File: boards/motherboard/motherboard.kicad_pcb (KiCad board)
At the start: 2 copper layers, 214.4 x 66 mm, 50 parts, among them J1 RJ45, J2 RJ45, J3 RJ45, J4 RJ45, J5 RJ45, U1 EBAYPCA9685

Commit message: another revision
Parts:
- added REF11: MountingHole_2-5mm, Mounting_Holes:MountingHole_2-5mm, F.Cu at (66.3, 49.5)
- 350ma1, 350ma10, 350ma11, 350ma12, 350ma13, 350ma14, 350ma15, 350ma2, 350ma3, 350ma4, 350ma5, 350ma6, 350ma7, 350ma8, 350ma9: footprint lighting:350ma constant current xl4001 -> lighting:350ma_constant_current_xl4001
- BLK1, BLK2: footprint lighting:TerminalBlock -> Connect:bornier2
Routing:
- net GNDPWR: track 100.2 -> 93.4 mm
- net +24V: track 98.8 -> 97.6 mm
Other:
- board text added: "0"
- board text added: "1"
- board text added: "2"
- board text added: "3"
- board text added: "4"

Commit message: minor fix
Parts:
- moved REF3 3.05 mm to (232.7, 49.5)
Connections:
- R12 pad 1: Net-(R12-Pad1) -> VCC
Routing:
- net /led0: track 77.0 -> 79.5 mm
- net VCC: track 273.6 -> 275.4 mm
- net /scl: track 73.0 -> 73.9 mm

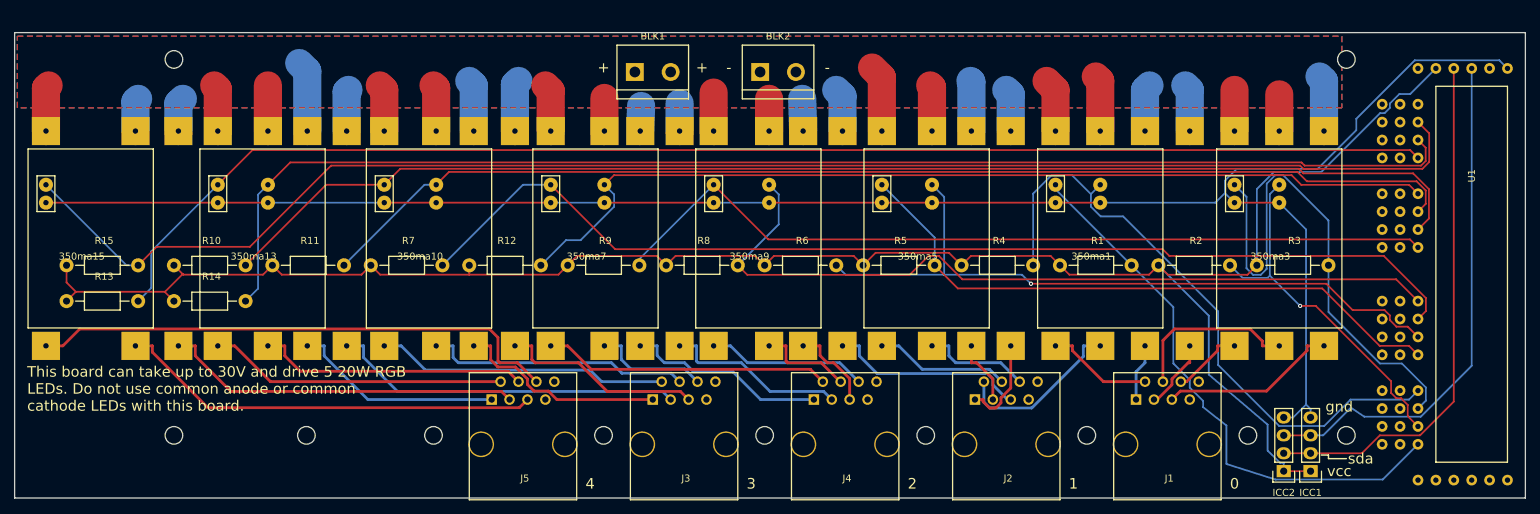
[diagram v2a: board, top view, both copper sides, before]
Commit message: added breakout for ethernet
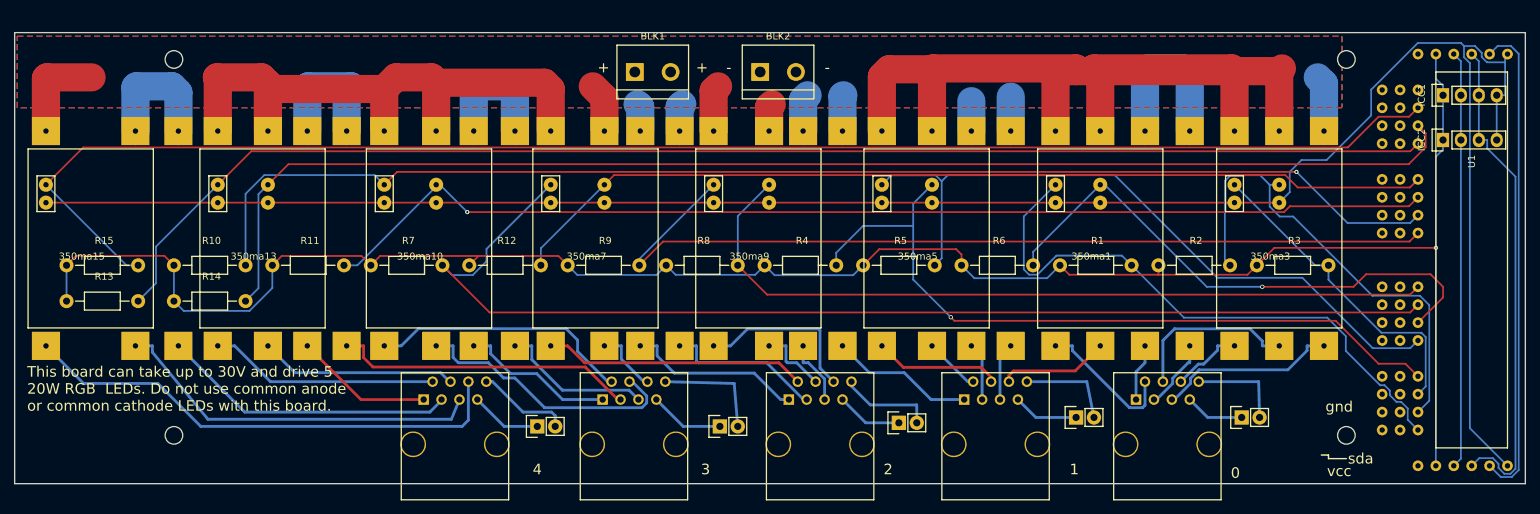
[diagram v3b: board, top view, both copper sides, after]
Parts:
- removed REF1, REF4, REF5, REF6, REF7, REF8, REF9: MountingHole_2-5mm, Mounting_Holes:MountingHole_2-5mm
- added CN1: CONN_01X02, Pin_Headers:Pin_Header_Straight_1x02, F.Cu at (217.8, 100.3)
- added CN2: CONN_01X02, Pin_Headers:Pin_Header_Straight_1x02, F.Cu at (194.3, 100.3)
- added CN3: CONN_01X02, Pin_Headers:Pin_Header_Straight_1x02, F.Cu at (143.8, 101.6)
- added CN4: CONN_01X02, Pin_Headers:Pin_Header_Straight_1x02, F.Cu at (169.2, 101.1)
- added CN5: CONN_01X02, Pin_Headers:Pin_Header_Straight_1x02, F.Cu at (117.9, 101.6)
- moved ICC1 56.6 mm to (246.4, 54.6), turned to 90 degrees
- moved ICC2 52.1 mm to (246.4, 61.0), turned to 90 degrees
- moved R4 27.9 mm to (150.1, 78.7)
- moved R6 27.9 mm to (178.1, 78.7)
- moved 350ma4 23.9 mm to (173.9, 90.2)
- moved 350ma6 23.9 mm to (197.7, 90.2)
- moved J5 9.65 mm to (106.2, 104.1)
- moved J3 7.11 mm to (131.6, 104.1)
- moved J4 3.56 mm to (158.0, 104.1)
- moved U1 2.03 mm to (237.7, 53.8)
- moved J2 1.52 mm to (182.9, 104.1)
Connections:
- U1 pad 17: Net-(U1-Pad17) -> V+
- U1 pad 23: (no net) -> V+
- U1 pad 24: (no net) -> VCC
- U1 pad 25: (no net) -> /sda
- U1 pad 26: (no net) -> /scl
- U1 pad 27: (no net) -> Net-(U1-Pad21)
- U1 pad 28: (no net) -> GND
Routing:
- net +24V: track 97.6 -> 246.6 mm
- net Net-(U1-Pad21): track 0.00 -> 69.3 mm
- net GND: track 262.7 -> 297.4 mm
- net /led2: track 74.8 -> 45.8 mm
- net /led5: track 100.6 -> 78.0 mm
- net GNDPWR: track 93.4 -> 114.3 mm
- net Net-(350ma6-Pad4): track 28.4 -> 8.25 mm
- net /led1: track 51.8 -> 68.3 mm, vias 1 -> 0
- net Net-(350ma4-Pad3): track 24.3 -> 7.95 mm
- net /led3: track 90.1 -> 106.2 mm, vias 0 -> 1
- net Net-(CN3-Pad2): track 0.00 -> 15.9 mm
- net /sda: track 74.4 -> 59.3 mm
- net Net-(CN2-Pad2): track 0.00 -> 13.7 mm
- net Net-(CN1-Pad2): track 0.00 -> 13.6 mm
- net Net-(CN4-Pad2): track 0.00 -> 13.6 mm
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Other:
- board size 214.4 x 66 mm -> 214.4 x 64 mm

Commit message: made a hole for capacitor
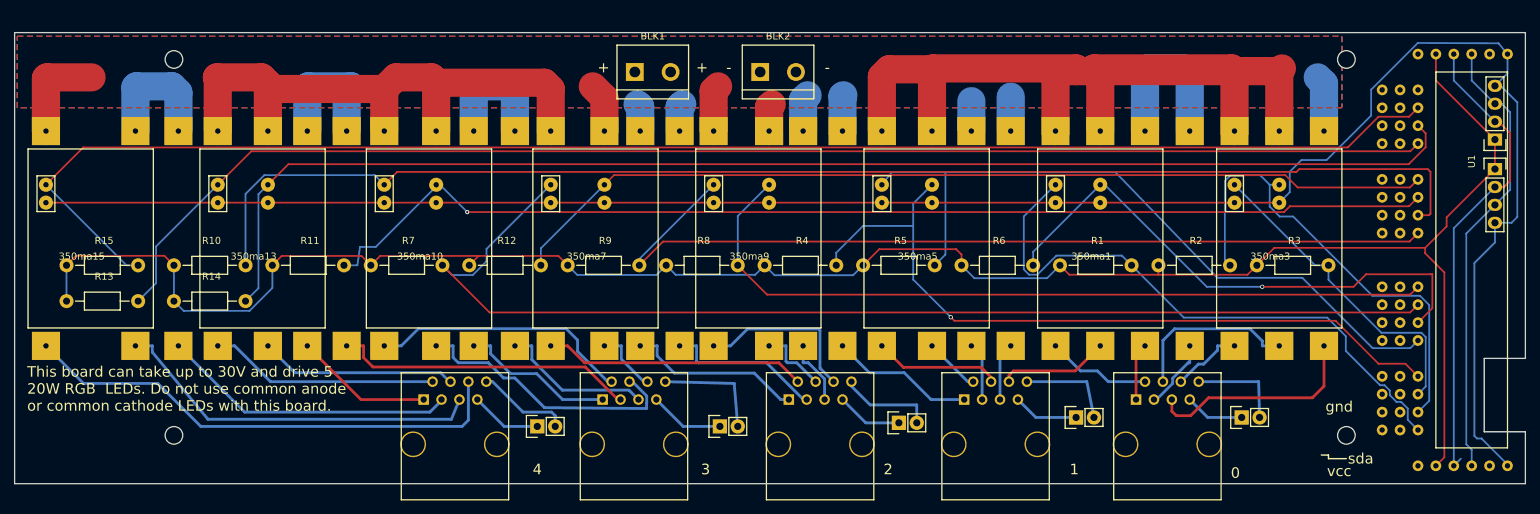
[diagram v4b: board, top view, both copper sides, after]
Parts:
- moved ICC1 9.68 mm to (253.7, 60.9), turned to 180 degrees
- moved ICC2 8.44 mm to (253.7, 65.1), turned to 0 degrees
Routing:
- net Net-(U1-Pad21): track 69.3 -> 0.00 mm
- net GND: track 297.4 -> 289.0 mm
- net /sda: track 59.3 -> 67.5 mm
- net VCC: track 285.2 -> 292.1 mm, vias 1 -> 0
- net /led9: track 182.4 -> 189.1 mm, vias 1 -> 0
- net /scl: track 70.3 -> 64.1 mm
- net Net-(350ma3-Pad4): track 25.6 -> 31.3 mm
- net Net-(350ma1-Pad3): track 20.2 -> 14.8 mm
- net /led4: track 100.3 -> 101.7 mm
- net /led10: track 159.7 -> 160.8 mm
- net /led5: track 78.0 -> 76.9 mm
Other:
- outline, holes or cut-outs redrawn

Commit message: sink
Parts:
- added BLK3: CONN_01X02, Connect:bornier2, F.Cu at (52.1, 105.9)
- REF10, REF11, REF2, REF3: value MountingHole_2-5mm -> MountingHole; footprint Mounting_Holes:MountingHole_2-5mm -> Mounting_Holes:MountingHole_3mm
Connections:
- CN1 pad 1: Net-(CN1-Pad1) -> /gnd2
- CN1 pad 2: Net-(CN1-Pad2) -> /vpwr2
- CN2 pad 1: Net-(CN2-Pad1) -> /gnd2
- CN2 pad 2: Net-(CN2-Pad2) -> /vpwr2
- CN3 pad 1: Net-(CN3-Pad1) -> /gnd2
- CN3 pad 2: Net-(CN3-Pad2) -> /vpwr2
- CN4 pad 1: Net-(CN4-Pad1) -> /gnd2
- CN4 pad 2: Net-(CN4-Pad2) -> /vpwr2
- CN5 pad 1: Net-(CN5-Pad1) -> /gnd2
- CN5 pad 2: Net-(CN5-Pad2) -> /vpwr2
- J1 pad 7: Net-(CN1-Pad1) -> /gnd2
- J1 pad 8: Net-(CN1-Pad2) -> /vpwr2
- J2 pad 7: Net-(CN2-Pad1) -> /gnd2
- J2 pad 8: Net-(CN2-Pad2) -> /vpwr2
- J3 pad 7: Net-(CN3-Pad1) -> /gnd2
- J3 pad 8: Net-(CN3-Pad2) -> /vpwr2
- J4 pad 7: Net-(CN4-Pad1) -> /gnd2
- J4 pad 8: Net-(CN4-Pad2) -> /vpwr2
- J5 pad 7: Net-(CN5-Pad1) -> /gnd2
- J5 pad 8: Net-(CN5-Pad2) -> /vpwr2
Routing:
- net /vpwr2: track 0.00 -> 123.1 mm
- net /gnd2: track 0.00 -> 80.7 mm
- net Net-(CN3-Pad2): track 15.9 -> 0.00 mm
- net Net-(CN2-Pad2): track 13.7 -> 0.00 mm
- net Net-(CN1-Pad2): track 13.6 -> 0.00 mm
- net Net-(CN4-Pad2): track 13.6 -> 0.00 mm
- net Net-(CN5-Pad2): track 13.3 -> 0.00 mm
- net /led0: track 84.0 -> 96.9 mm
- net Net-(CN3-Pad1): track 10.6 -> 0.00 mm
- net Net-(CN5-Pad1): track 10.1 -> 0.00 mm
- net Net-(CN4-Pad1): track 9.37 -> 0.00 mm
- net Net-(CN2-Pad1): track 9.31 -> 0.00 mm
- net Net-(CN1-Pad1): track 8.42 -> 0.00 mm
- net /led2: track 45.8 -> 53.5 mm
- net Net-(350ma9-Pad3): track 24.2 -> 19.2 mm
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- added copper zone on F.Cu, net /gnd2
- added copper zone on B.Cu, net /vpwr2
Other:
- board text added: "scl"
- board text added: "v2+"
- board text added: "v2-"

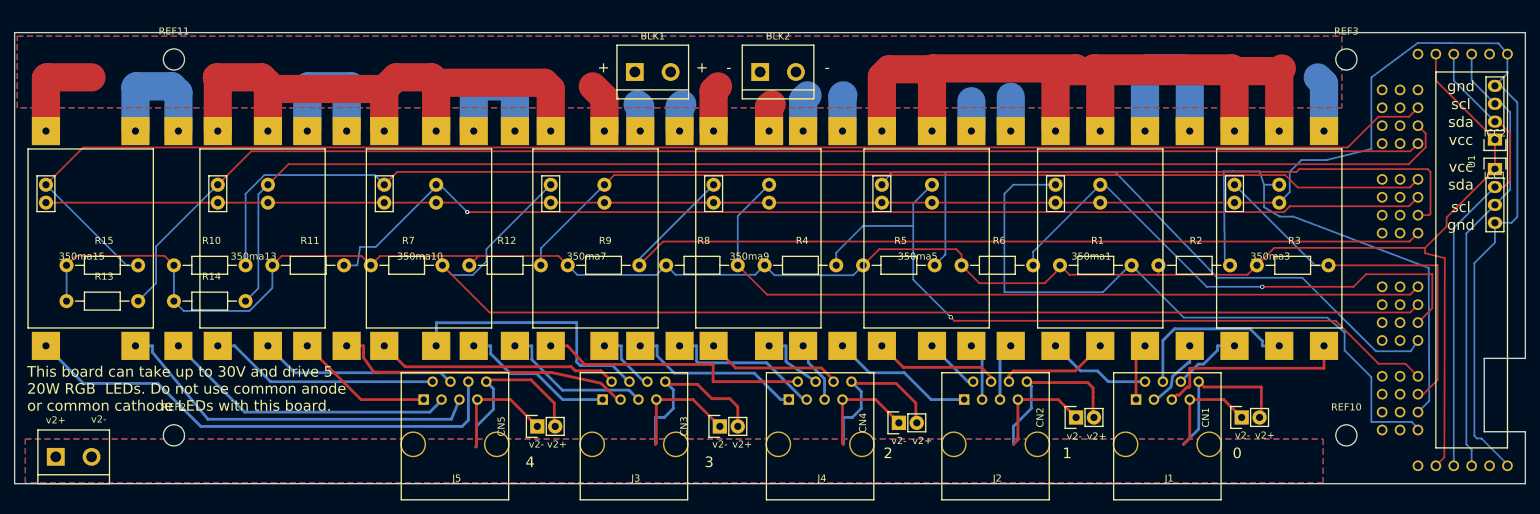
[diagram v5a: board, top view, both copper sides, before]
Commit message: no vias
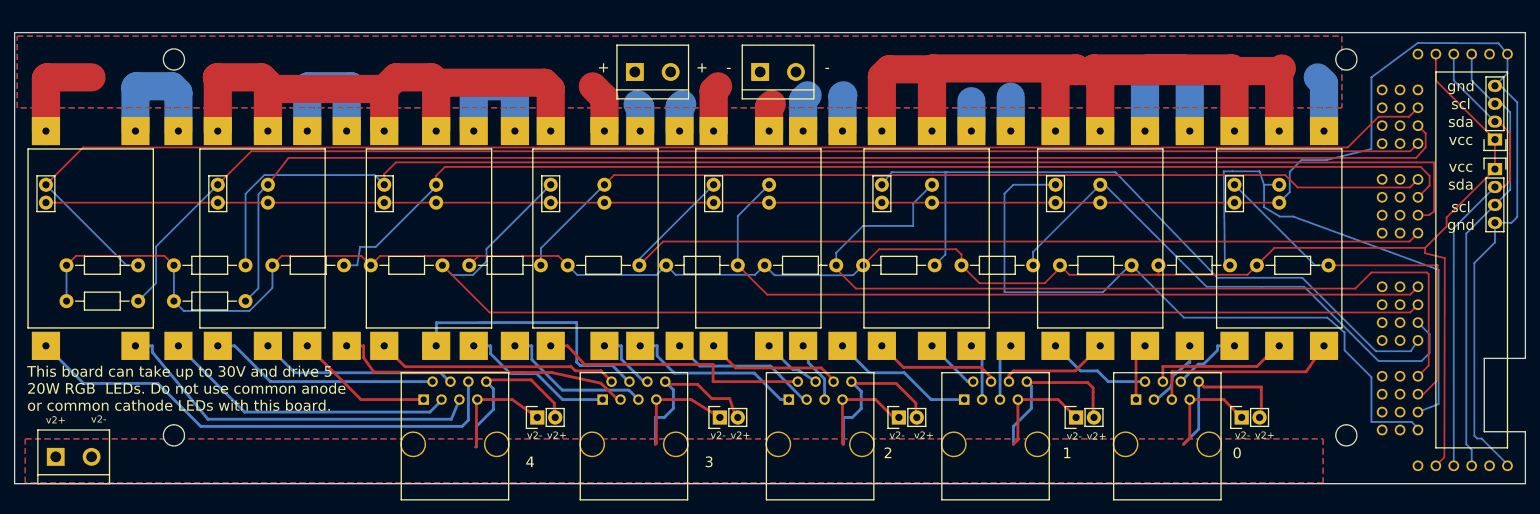
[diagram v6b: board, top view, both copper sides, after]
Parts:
- moved CN3 1.27 mm to (143.8, 100.3)
- moved CN5 1.27 mm to (117.9, 100.3)
- moved CN4 0.76 mm to (169.2, 100.3)
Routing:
- net /led3: track 106.2 -> 123.1 mm, vias 1 -> 0
- net /led10: track 160.8 -> 166.9 mm, vias 1 -> 0
- net Net-(350ma2-Pad3): track 24.4 -> 19.9 mm
- net /led9: track 189.1 -> 192.1 mm
- net /vpwr2: track 123.1 -> 120.2 mm
- net /led1: track 72.2 -> 74.7 mm
- net /gnd2: track 80.7 -> 79.1 mm
- net Net-(350ma8-Pad4): track 22.5 -> 21.2 mm
- net Net-(350ma8-Pad3): track 9.71 -> 8.59 mm
- net /led5: track 76.9 -> 77.9 mm, vias 1 -> 0
- net Net-(350ma3-Pad4): track 28.5 -> 27.8 mm

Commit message: minor changes
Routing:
- net /led13: track 188.2 -> 189.8 mm
- net /led9: track 192.1 -> 193.7 mm
- net VCC: track 293.9 -> 295.5 mm
- net /led1: track 74.7 -> 76.2 mm
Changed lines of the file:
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@@
   (segment (start 220.345 65.405) (end 220.98 67.31) (width 0.25) (layer B.Cu) (net 9))
   (segment (start 216.535 65.405) (end 220.345 65.405) (width 0.25) (layer B.Cu) (net 9))
-  (segment (start 215.265 65.405) (end 216.535 65.405) (width 0.25) (layer B.Cu) (net 9))
-  (segment (start 215.4196 78.0056) (end 215.265 65.405) (width 0.25) (layer B.Cu) (net 9))
-  (segment (start 216.154 78.74) (end 215.4196 78.0056) (width 0.25) (layer B.Cu) (net 9))
+  (segment (start 214.503 65.405) (end 216.535 65.405) (width 0.25) (layer B.Cu) (net 9))
+  (segment (start 214.503 77.978) (end 214.503 65.405) (width 0.25) (layer B.Cu) (net 9))
+  (segment (start 216.154 78.74) (end 214.503 77.978) (width 0.25) (layer B.Cu) (net 9))
   (segment (start 245.745 98.425) (end 242.824 99.568) (width 0.25) (layer B.Cu) (net 9))
   (segment (start 245.745 79.375) (end 245.745 98.425) (width 0.25) (layer B.Cu) (net 9))
@@
   (segment (start 97.79 64.135) (end 96.139 65.786) (width 0.25) (layer F.Cu) (net 31))
   (segment (start 76.454 68.608) (end 76.454 78.74) (width 0.25) (layer B.Cu) (net 31))
-  (segment (start 79.1224 65.9396) (end 76.454 68.608) (width 0.25) (layer B.Cu) (net 31))
-  (segment (start 94.7686 65.9396) (end 79.1224 65.9396) (width 0.25) (layer B.Cu) (net 31))
+  (segment (start 76.454 65.913) (end 76.454 68.608) (width 0.25) (layer B.Cu) (net 31))
+  (segment (start 94.7686 65.9396) (end 76.454 65.913) (width 0.25) (layer B.Cu) (net 31))
   (segment (start 96.139 67.31) (end 94.7686 65.9396) (width 0.25) (layer B.Cu) (net 31))
   (segment (start 103.549537 90.125463) (end 103.549537 86.884895) (width 0.4) (layer B.Cu) (net 32))
@@
   (segment (start 63.7541 76.0729) (end 63.7541 81.2799) (width 0.25) (layer B.Cu) (net 40))
   (segment (start 72.517 67.31) (end 63.7541 76.0729) (width 0.25) (layer B.Cu) (net 40))
-  (segment (start 241.7366 62.5554) (end 242.824 61.468) (width 0.25) (layer F.Cu) (net 40))
-  (segment (start 77.2716 62.5554) (end 241.7366 62.5554) (width 0.25) (layer F.Cu) (net 40))
-  (segment (start 72.517 67.31) (end 77.2716 62.5554) (width 0.25) (layer F.Cu) (net 40))
+  (segment (start 241.808 62.992) (end 242.824 61.468) (width 0.25) (layer F.Cu) (net 40))
+  (segment (start 77.216 62.992) (end 241.808 62.992) (width 0.25) (layer F.Cu) (net 40))
+  (segment (start 72.517 67.31) (end 77.216 62.992) (width 0.25) (layer F.Cu) (net 40))
   (segment (start 105.537 95.25) (end 105.41 95.25) (width 0.4) (layer B.Cu) (net 41))
   (segment (start 105.41 95.25) (end 104.14 93.98) (width 0.4) (layer B.Cu) (net 41))
@@
   (segment (start 79.629 67.31) (end 78.2866 68.6524) (width 0.25) (layer B.Cu) (net 43))
   (segment (start 79.629 67.31) (end 82.55 63.5) (width 0.25) (layer F.Cu) (net 43))
-  (segment (start 243.9134 60.0174) (end 242.824 58.928) (width 0.25) (layer F.Cu) (net 43))
-  (segment (start 243.9134 61.9891) (end 243.9134 60.0174) (width 0.25) (layer F.Cu) (net 43))
-  (segment (start 242.57 63.5) (end 243.9134 61.9891) (width 0.25) (layer F.Cu) (net 43))
+  (segment (start 244.348 59.944) (end 242.824 58.928) (width 0.25) (layer F.Cu) (net 43))
+  (segment (start 244.348 63.5) (end 244.348 59.944) (width 0.25) (layer F.Cu) (net 43))
+  (segment (start 242.57 63.5) (end 244.348 63.5) (width 0.25) (layer F.Cu) (net 43))
   (segment (start 82.55 63.5) (end 242.57 63.5) (width 0.25) (layer F.Cu) (net 43))
   (segment (start 108.077 95.25) (end 108.077 100.711) (width 0.4) (layer B.Cu) (net 44))
@@
   (segment (start 59.563 78.74) (end 61.214 78.74) (width 0.25) (layer B.Cu) (net 46))
   (segment (start 48.133 67.31) (end 59.563 78.74) (width 0.25) (layer B.Cu) (net 46))
-  (segment (start 53.4276 62.0154) (end 48.133 67.31) (width 0.25) (layer F.Cu) (net 46))
-  (segment (start 232.8658 62.0154) (end 53.4276 62.0154) (width 0.25) (layer F.Cu) (net 46))
-  (segment (start 237.2232 57.658) (end 232.8658 62.0154) (width 0.25) (layer F.Cu) (net 46))
+  (segment (start 53.34 62.484) (end 48.133 67.31) (width 0.25) (layer F.Cu) (net 46))
+  (segment (start 232.918 62.484) (end 53.34 62.484) (width 0.25) (layer F.Cu) (net 46))
+  (segment (start 237.2232 57.658) (end 232.918 62.484) (width 0.25) (layer F.Cu) (net 46))
   (segment (start 241.554 57.658) (end 237.2232 57.658) (width 0.25) (layer F.Cu) (net 46))
   (segment (start 242.824 56.388) (end 241.554 57.658) (width 0.25) (layer F.Cu) (net 46))
+  (segment (start 66.294 83.82) (end 66.294 78.74) (width 0.25) (layer F.Cu) (net 47))
+  (segment (start 51.054 83.82) (end 51.054 78.74) (width 0.25) (layer F.Cu) (net 47))
+  (segment (start 80.264 78.74) (end 80.264 83.312) (width 0.25) (layer F.Cu) (net 47))
+  (segment (start 68.58 86.106) (end 66.294 83.82) (width 0.25) (layer F.Cu) (net 47))
+  (segment (start 77.47 86.106) (end 68.58 86.106) (width 0.25) (layer F.Cu) (net 47))
+  (segment (start 80.264 83.312) (end 77.47 86.106) (width 0.25) (layer F.Cu) (net 47))
   (segment (start 192.024 78.74) (end 192.024 79.121) (width 0.25) (layer F.Cu) (net 47))
   (segment (start 192.024 79.121) (end 189.865 81.28) (width 0.25) (layer F.Cu) (net 47))
@@
   (segment (start 177.292 76.454) (end 166.37 76.454) (width 0.25) (layer F.Cu) (net 47))
   (segment (start 178.054 77.216) (end 177.292 76.454) (width 0.25) (layer F.Cu) (net 47))
-  (segment (start 51.054 78.74) (end 51.054 83.82) (width 0.25) (layer B.Cu) (net 47))
   (segment (start 64.9499 77.3959) (end 66.294 78.74) (width 0.25) (layer F.Cu) (net 47))
+  (segment (start 51.054 78.74) (end 52.3981 77.3959) (width 0.25) (layer F.Cu) (net 47))
   (segment (start 52.3981 77.3959) (end 64.9499 77.3959) (width 0.25) (layer F.Cu) (net 47))
-  (segment (start 51.054 78.74) (end 52.3981 77.3959) (width 0.25) (layer F.Cu) (net 47))
-  (segment (start 66.294 83.82) (end 66.294 78.74) (width 0.25) (layer B.Cu) (net 47))
-  (segment (start 80.264 81.9569) (end 80.264 78.74) (width 0.25) (layer B.Cu) (net 47))
-  (segment (start 77.014 85.2069) (end 80.264 81.9569) (width 0.25) (layer B.Cu) (net 47))
-  (segment (start 67.6809 85.2069) (end 77.014 85.2069) (width 0.25) (layer B.Cu) (net 47))
-  (segment (start 66.294 83.82) (end 67.6809 85.2069) (width 0.25) (layer B.Cu) (net 47))
   (segment (start 108.204 78.74) (end 109.5289 77.4151) (width 0.25) (layer F.Cu) (net 47))
   (segment (start 120.8491 77.4151) (end 109.5289 77.4151) (width 0.25) (layer F.Cu) (net 47))
@@
     (polygon
       (pts
-        (xy 229.362 109.601) (xy 45.212 109.601) (xy 45.212 103.378) (xy 229.362 103.378) (xy 229.362 109.601)
+        (xy 45.212 109.601) (xy 45.212 103.378) (xy 216.408 103.378) (xy 216.408 109.601)
       )
     )
@@
     (polygon
       (pts
-        (xy 229.362 109.601) (xy 45.212 109.601) (xy 45.212 103.378) (xy 229.362 103.378) (xy 229.362 109.601)
+        (xy 45.212 109.601) (xy 45.212 103.378) (xy 216.408 103.378) (xy 216.408 109.601)
       )
     )
